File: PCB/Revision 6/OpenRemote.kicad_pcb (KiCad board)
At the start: 2 copper layers, 192.4 x 50 mm, 196 parts, among them J1 USB_C_Receptacle_USB2.0, J2 Conn_01x50, J3 JST_PH_B2B-PH, J4 2.54x2 Header, J5 Micro_SD_Card, J6 ER-CON06HB-1_TOUCH, J7 JST_PH_B2B-PH, Q1 DMG2301L, Q2 MBT3904DW1, Q3 DMG2301L, Q4 DMG2301L, Q5 DMG2301L, Q6 FS8205A, Q7 DMG2301L, U1 DW01A, U10 APX803S, U11 TP4056, U12 TCA8418, U2 XC6220B331, U3 CH340C, U4 USBLC6-2P6, U5 LIS3DHTR, U6 TSSP77038, U7 ESP32-S3-WROOM-1-N16R8, U8 AP2112K-3.3, U9 MAX17048G

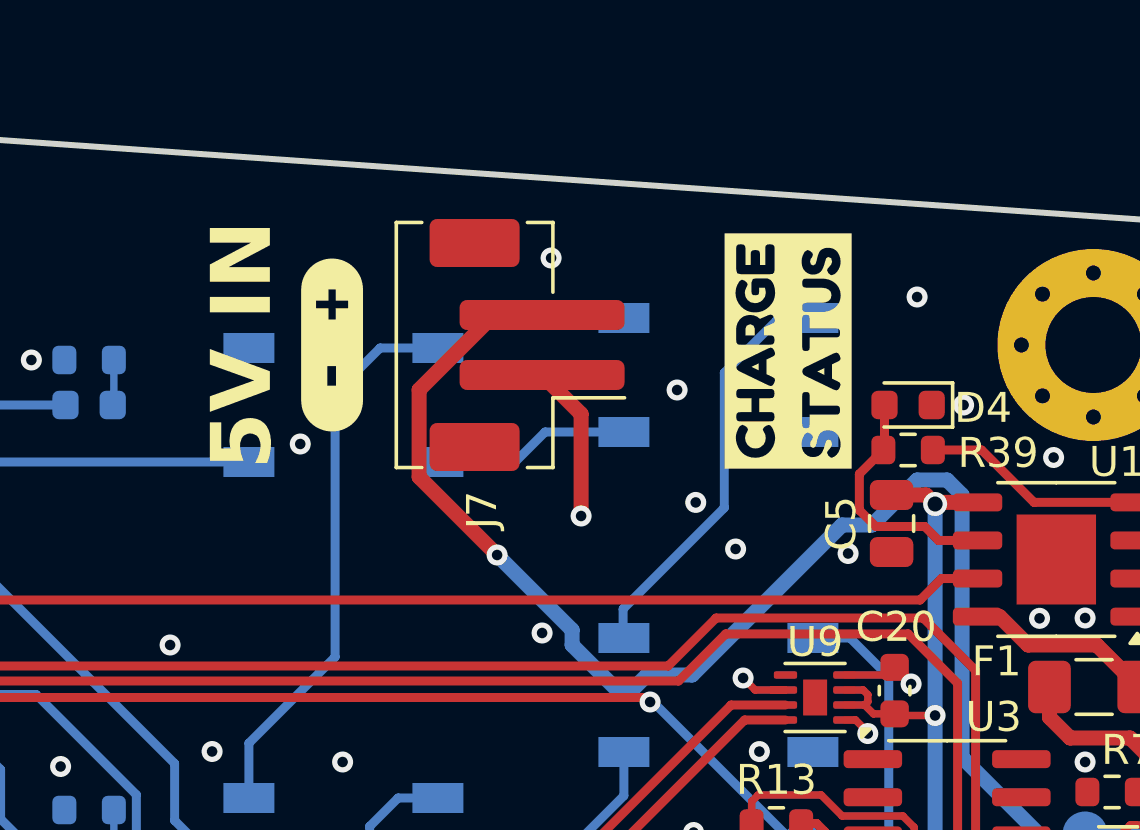
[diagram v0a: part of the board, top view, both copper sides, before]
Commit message: Relocate J7 5V-in connector, reroute, and regenerate gerbers
J7 moved from (214.000, 85.000, 90) to (218.500, 88.500, 90) - 4.5 mm
right, 3.5 mm down - with its VUSB_RAW and GND routing redone and two
GND vias relocated. A kibuzzard silkscreen label moved from
(222.700, 85.200, 90) to (224.500, 84.000, 0).

This clears both sub-spec clearances that were around J7:
  - J7 pad 1 (GND) to /VUSB_RAW  was 0.1049 mm  - gone
  - J7 pad MP to /VUSB_RAW       was 0.1000 mm  - gone

DRC errors 44 -> 41, clearance violations 11 -> 8.

Regenerated gerber.zip. Changed layers: F.Cu, B.Cu, F.Mask, F.Paste and
both silkscreens. Mask (back), paste (back), edge cuts and both drill
files are identical plots.

NOTE: CPL.csv is now wrong for J7 - it still carries the old 214.0/85.0
position. It must be regenerated before any assembly order.

Co-Authored-By: Claude Opus 5 <noreply@anthropic.com>
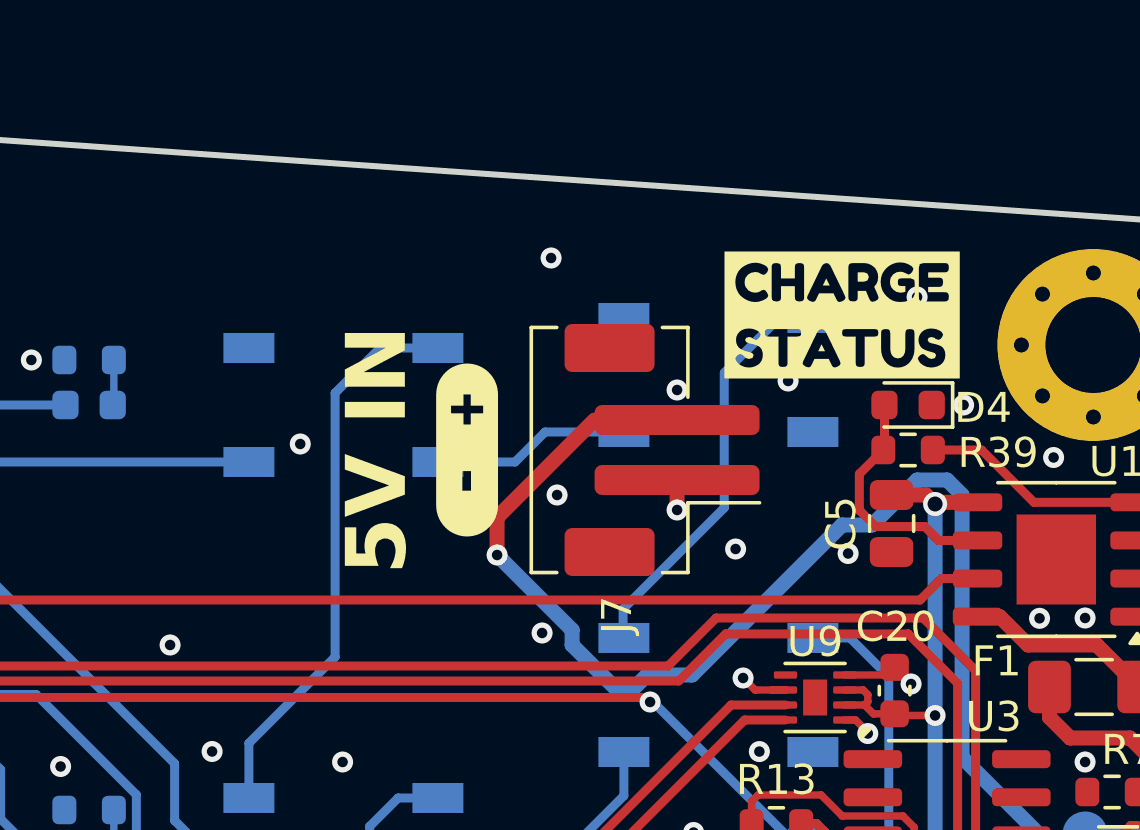
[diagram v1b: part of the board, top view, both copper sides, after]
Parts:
- moved J7 5.70 mm to (218.5, 88.5)
- moved kibuzzard-63D97EAF 5.70 mm to (212.0, 88.5)
- moved kibuzzard-643EE600 2.16 mm to (224.5, 84.0), turned to 0 degrees
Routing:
- net GND: track 96.7 -> 92.4 mm
- net /VUSB_RAW: track 64.8 -> 61.7 mm
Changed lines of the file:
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@@
 	(footprint "kibuzzard-643EE600"
 		(layer "F.Cu")
-		(at 222.7 85.2 90)
+		(at 224.5 84)
 		(descr "Generated with KiBuzzard")
 		(tags "kb_params=eyJBbGlnbm1lbnRDaG9pY2UiOiAiUmlnaHQiLCAiQ2FwTGVmdENob2ljZSI6ICJbIiwgIkNhcFJpZ2h0Q2hvaWNlIjogIl0iLCAiRm9udENvbWJvQm94IjogIkZyZWRva2FPbmUiLCAiSGVpZ2h0Q3RybCI6ICIxLjEiLCAiTGF5ZXJDb21ib0JveCI6ICJGLlNpbGtTIiwgIk11bHRpTGluZVRleHQiOiAiQ0hBUkdFXHJcblNUQVRVUyIsICJQYWRkaW5nQm90dG9tQ3RybCI6ICI1IiwgIlBhZGRpbmdMZWZ0Q3RybCI6ICI1IiwgIlBhZGRpbmdSaWdodEN0cmwiOiAiNSIsICJQYWRkaW5nVG9wQ3RybCI6ICI1IiwgIldpZHRoQ3RybCI6ICIxIn0=")
 		(property "Reference" "kibuzzard-643EE600"
-			(at 0 -5.164882 90)
+			(at 0 -5.164882 0)
 			(layer "F.SilkS")
 			(hide yes)
@@
 		)
 		(property "Value" "G***"
-			(at 0 5.164882 90)
+			(at 0 5.164882 0)
 			(layer "F.SilkS")
 			(hide yes)
@@
 		)
 		(property "Datasheet" ""
-			(at 0 0 90)
+			(at 0 0 0)
 			(unlocked yes)
 			(layer "F.Fab")
@@
 		)
 		(property "Description" ""
-			(at 0 0 90)
+			(at 0 0 0)
 			(unlocked yes)
 			(layer "F.Fab")
@@
 		(fp_poly
 			(pts
-				(xy -0.528791 -1.220474) (xy -0.644044 -0.981238) (xy -0.411792 -0.981238) (xy -0.528791 -1.220474)
+				(xy -0.684319 0.973719) (xy -0.797869 1.20942) (xy -0.56905 1.20942) (xy -0.684319 0.973719)
 			)
 			(stroke
@@
 		(fp_poly
 			(pts
-				(xy -0.684319 0.973719) (xy -0.797869 1.20942) (xy -0.56905 1.20942) (xy -0.684319 0.973719)
+				(xy -0.528791 -1.220474) (xy -0.644044 -0.981238) (xy -0.411792 -0.981238) (xy -0.528791 -1.220474)
 			)
 			(stroke
@@
 	(footprint "OpenRemoteLib:JST_PH_B2B-PH-SM4-TB_1x02-1MP_P2.00mm_Vertical"
 		(layer "F.Cu")
-		(at 214 85 90)
+		(at 218.5 88.5 90)
 		(descr "JST PH series connector, B2B-PH-SM4-TB (http://www.jst-mfg.com/product/pdf/eng/ePH.pdf), generated with kicad-footprint-generator")
 		(tags "connector JST PH side entry")
@@
 	(footprint "kibuzzard-63D97EAF"
 		(layer "F.Cu")
-		(at 207.5 85 -90)
+		(at 212 88.5 -90)
 		(descr "Generated with KiBuzzard")
 		(tags "kb_params=eyJBbGlnbm1lbnRDaG9pY2UiOiAiQ2VudGVyIiwgIkNhcExlZnRDaG9pY2UiOiAiKCIsICJDYXBSaWdodENob2ljZSI6ICIpIiwgIkZvbnRDb21ib0JveCI6ICJVYnVudHVNb25vLUIiLCAiSGVpZ2h0Q3RybCI6ICIxLjUiLCAiTGF5ZXJDb21ib0JveCI6ICJGLlNpbGtTIiwgIk11bHRpTGluZVRleHQiOiAiKyAtIiwgIlBhZGRpbmdCb3R0b21DdHJsIjogIjUiLCAiUGFkZGluZ0xlZnRDdHJsIjogIjAiLCAiUGFkZGluZ1JpZ2h0Q3RybCI6ICI1IiwgIlBhZGRpbmdUb3BDdHJsIjogIjUiLCAiV2lkdGhDdHJsIjogIjAuNCJ9")
@@
 	)
 	(gr_text "5V IN"
-		(at 204.5 85 90)
+		(at 209 88.5 90)
 		(layer "F.SilkS")
 		(effects
@@
 	)
 	(segment
-		(start 215.8 87.3)
-		(end 215.8 90.7)
-		(width 0.5)
-		(layer "F.Cu")
-		(net "GND")
-	)
-	(segment
 		(start 234.275 111.8)
 		(end 233.8 112.275)
@@
 	)
 	(segment
-		(start 214.5 86)
-		(end 215.8 87.3)
-		(width 0.5)
-		(layer "F.Cu")
-		(net "GND")
-	)
-	(segment
 		(start 224.95 97.5)
 		(end 224.5875 97.5)
@@
 	)
 	(segment
+		(start 219 89.5)
+		(end 219 90.5)
+		(width 0.5)
+		(layer "F.Cu")
+		(net "GND")
+	)
+	(segment
 		(start 99.525 93.25)
 		(end 102.012852 93.25)
@@
 	)
 	(via
-		(at 219.620975 90.247653)
+		(at 219 90.5)
 		(size 0.7)
 		(drill 0.35)
@@
 	)
 	(via
-		(at 215.8 90.7)
+		(at 215 90)
 		(size 0.7)
 		(drill 0.35)
@@
 	)
 	(segment
-		(start 235.469165 104.45)
-		(end 235.458662 104.439497)
-		(width 0.25)
+		(start 213 92)
+		(end 213 90.75)
+		(width 0.5)
 		(layer "F.Cu")
 		(net "/VUSB_RAW")
 	)
 	(segment
-		(start 214.5 84)
-		(end 212.894544 84)
-		(width 0.3)
+		(start 235.469165 104.45)
+		(end 235.458662 104.439497)
+		(width 0.25)
 		(layer "F.Cu")
 		(net "/VUSB_RAW")
@@
 	)
 	(segment
-		(start 210.4 89.4)
-		(end 213 92)
-		(width 0.5)
-		(layer "F.Cu")
-		(net "/VUSB_RAW")
-	)
-	(segment
 		(start 236.955 104.45)
 		(end 235.469165 104.45)
@@
 	)
 	(segment
-		(start 212.894544 84)
-		(end 210.4 86.494544)
-		(width 0.5)
+		(start 216.25 87.5)
+		(end 219 87.5)
+		(width 0.3)
 		(layer "F.Cu")
 		(net "/VUSB_RAW")
 	)
 	(segment
-		(start 234.1 98.1)
-		(end 232.1 98.1)
+		(start 213 90.75)
+		(end 216.25 87.5)
 		(width 0.5)
 		(layer "F.Cu")
@@
 	)
 	(segment
-		(start 210.4 86.494544)
-		(end 210.4 89.4)
+		(start 234.1 98.1)
+		(end 232.1 98.1)
 		(width 0.5)
 		(layer "F.Cu")

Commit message: Shorten J6 touch connector silkscreen label and regenerate gerbers
J6 value field on F.SilkS changed from "ER-CON06HB-1_TOUCH" to "Touch".
No electrical change: 1519 track segments and 355 vias match the previous
commit as sets, and no footprint moved.

Regenerated gerber.zip. F.Silkscreen is the only layer that differs
(-242 plot operations, consistent with the shorter string); F.Cu, B.Cu,
both masks, both pastes, edge cuts, both drill files and the job file are
identical plots.

Also adds the v33 rear case STLs (pogo and no-pogo) and a read-only
Fusion script, OpenRemoteRev6LipDiagnose, for tracing the missing
outer-lip feature (Sketch39 / Extrude45).

Co-Authored-By: Claude Opus 5 <noreply@anthropic.com>
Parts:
- J6: value ER-CON06HB-1_TOUCH -> Touch
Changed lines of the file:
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@@
 			)
 		)
-		(property "Value" "ER-CON06HB-1_TOUCH"
+		(property "Value" "Touch"
 			(at 0 5.95 90)
 			(layer "F.SilkS")
